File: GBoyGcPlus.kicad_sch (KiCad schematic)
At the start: 45 parts, among them J2 Conn_01x06, J3 Left Stick, J4 Right Stick, SW1 RKA2SGG055SMTR LFS, SW2 RKA2SGG055SMTR LFS, SW3 RKA2SGG055SMTR LFS, SW4 RKA2SGG055SMTR LFS, SW5 RKA2SGG055SMTR LFS, SW6 RKA2SGG055SMTR LFS, SW7 RKA2SGG055SMTR LFS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

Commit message: Schematic only
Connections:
- net +3V3: now also J3.1, J4.1; no longer J3.5, J4.5
- net CX: now also J4.5; no longer J4.1
- net CY: now also J4.2; no longer J4.4
- net GND: now also J3.4, J4.4; no longer J3.2, J4.2
- net SX: now also J3.5; no longer J3.1
- net SY: now also J3.2; no longer J3.4
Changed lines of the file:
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@@
     (effects (font (size 1.27 1.27)) (justify left bottom))
   )
-  (label "SY" (at 556.26 375.92 90) (fields_autoplaced)
+  (label "SY" (at 551.18 378.46 0) (fields_autoplaced)
     (effects (font (size 1.27 1.27)) (justify left bottom))
   )
@@
     (effects (font (size 1.27 1.27)) (justify left bottom))
   )
-  (label "CY" (at 595.63 375.92 90) (fields_autoplaced)
+  (label "CY" (at 590.55 378.46 0) (fields_autoplaced)
     (effects (font (size 1.27 1.27)) (justify left bottom))
   )
@@
     (effects (font (size 1.27 1.27)) (justify left bottom))
   )
-  (label "SX" (at 548.64 375.92 90) (fields_autoplaced)
+  (label "SX" (at 558.8 379.73 0) (fields_autoplaced)
     (effects (font (size 1.27 1.27)) (justify left bottom))
   )
@@
     (effects (font (size 1.27 1.27)) (justify left bottom))
   )
-  (label "CX" (at 588.01 375.92 90) (fields_autoplaced)
+  (label "CX" (at 598.17 378.46 0) (fields_autoplaced)
     (effects (font (size 1.27 1.27)) (justify left bottom))
   )
@@
     )
   )
-  (symbol (lib_id "power:+3V3") (at 598.17 378.46 180) (unit 1)
-    (in_bom yes) (on_board yes) (dnp no) (fields_autoplaced)
-    (property "Reference" "#PWR09" (at 598.17 374.65 0)
-      (effects (font (size 1.27 1.27)) hide)
-    )
-    (property "Value" "+3V3" (at 598.17 383.54 0)
-      (effects (font (size 1.27 1.27)))
-    )
-    (property "Footprint" "" (at 598.17 378.46 0)
-      (effects (font (size 1.27 1.27)) hide)
-    )
-    (property "Datasheet" "" (at 598.17 378.46 0)
+  (symbol (lib_id "power:+3V3") (at 588.01 375.92 180) (unit 1)
+    (in_bom yes) (on_board yes) (dnp no) (fields_autoplaced)
+    (property "Reference" "#PWR09" (at 588.01 372.11 0)
+      (effects (font (size 1.27 1.27)) hide)
+    )
+    (property "Value" "+3V3" (at 588.01 381 0)
+      (effects (font (size 1.27 1.27)))
+    )
+    (property "Footprint" "" (at 588.01 375.92 0)
+      (effects (font (size 1.27 1.27)) hide)
+    )
+    (property "Datasheet" "" (at 588.01 375.92 0)
       (effects (font (size 1.27 1.27)) hide)
     )
@@
     )
   )
-  (symbol (lib_id "power:GND") (at 551.18 378.46 0) (unit 1)
-    (in_bom yes) (on_board yes) (dnp no) (fields_autoplaced)
-    (property "Reference" "#PWR06" (at 551.18 384.81 0)
-      (effects (font (size 1.27 1.27)) hide)
-    )
-    (property "Value" "GND" (at 551.18 383.54 0)
-      (effects (font (size 1.27 1.27)))
-    )
-    (property "Footprint" "" (at 551.18 378.46 0)
-      (effects (font (size 1.27 1.27)) hide)
-    )
-    (property "Datasheet" "" (at 551.18 378.46 0)
+  (symbol (lib_id "power:GND") (at 556.26 375.92 0) (unit 1)
+    (in_bom yes) (on_board yes) (dnp no) (fields_autoplaced)
+    (property "Reference" "#PWR06" (at 556.26 382.27 0)
+      (effects (font (size 1.27 1.27)) hide)
+    )
+    (property "Value" "GND" (at 556.26 381 0)
+      (effects (font (size 1.27 1.27)))
+    )
+    (property "Footprint" "" (at 556.26 375.92 0)
+      (effects (font (size 1.27 1.27)) hide)
+    )
+    (property "Datasheet" "" (at 556.26 375.92 0)
       (effects (font (size 1.27 1.27)) hide)
     )
@@
     )
   )
-  (symbol (lib_id "power:+3V3") (at 558.8 379.73 180) (unit 1)
-    (in_bom yes) (on_board yes) (dnp no) (fields_autoplaced)
-    (property "Reference" "#PWR07" (at 558.8 375.92 0)
-      (effects (font (size 1.27 1.27)) hide)
-    )
-    (property "Value" "+3V3" (at 558.8 384.81 0)
-      (effects (font (size 1.27 1.27)))
-    )
-    (property "Footprint" "" (at 558.8 379.73 0)
-      (effects (font (size 1.27 1.27)) hide)
-    )
-    (property "Datasheet" "" (at 558.8 379.73 0)
+  (symbol (lib_id "power:+3V3") (at 548.64 375.92 180) (unit 1)
+    (in_bom yes) (on_board yes) (dnp no) (fields_autoplaced)
+    (property "Reference" "#PWR07" (at 548.64 372.11 0)
+      (effects (font (size 1.27 1.27)) hide)
+    )
+    (property "Value" "+3V3" (at 548.64 381 0)
+      (effects (font (size 1.27 1.27)))
+    )
+    (property "Footprint" "" (at 548.64 375.92 0)
+      (effects (font (size 1.27 1.27)) hide)
+    )
+    (property "Datasheet" "" (at 548.64 375.92 0)
       (effects (font (size 1.27 1.27)) hide)
     )
@@
     )
   )
-  (symbol (lib_id "power:GND") (at 590.55 378.46 0) (unit 1)
-    (in_bom yes) (on_board yes) (dnp no) (fields_autoplaced)
-    (property "Reference" "#PWR08" (at 590.55 384.81 0)
-      (effects (font (size 1.27 1.27)) hide)
-    )
-    (property "Value" "GND" (at 590.55 383.54 0)
-      (effects (font (size 1.27 1.27)))
-    )
-    (property "Footprint" "" (at 590.55 378.46 0)
-      (effects (font (size 1.27 1.27)) hide)
-    )
-    (property "Datasheet" "" (at 590.55 378.46 0)
-      (effects (font (size 1.27 1.27)) hide)
-    )
+  (symbol (lib_id "power:GND") (at 595.63 375.92 0) (unit 1)
+    (in_bom yes) (on_board yes) (dnp no) (fields_autoplaced)
+    (property "Reference" "#PWR08" (at 595.63 382.27 0)
+      (effects (font (size 1.27 1.27)) hide)
+    )
+    (property "Value" "GND" (at 595.63 381 0)
+      (effects (font (size 1.27 1.27)))
+    )
+    (property "Footprint" "" (at 595.63 375.92 0)
+      (effects (font (size 1.27 1.27)) hide)
+    )
+    (property "Datasheet" "" (at 595.63 375.92 0)
+      (effects (font (size 1.27 1.27)) hide)
+    )

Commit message: Added gerber files
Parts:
- removed TP6, TP7, TP8: TestPoint, TestPoint:TestPoint_Pad_D1.0mm, symbol Connector:TestPoint
- added J1: Conn_01x06, Connector_PinSocket_1.27mm:PinSocket_1x06_P1.27mm_Vertical, symbol Connector_Generic:Conn_01x06
- U1: footprint GCPlus:SSOP28_MC_MCH-L -> GCPlus:SSOP28_MC_MCH
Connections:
- net +3V3: now also J1.2 (Pin_2)
- net DD: no longer SW7.2
- net DL: no longer SW5.2
- net DR: no longer SW6.2
- net DU: no longer SW8.2
- net GND: now also J1.3 (Pin_3); no longer SW5.4, SW6.4, SW7.4, SW8.4
- net MCLR: now also J1.1 (Pin_1)
- net PGC: now also J1.5 (Pin_5)
- net PGD: now also J1.4 (Pin_4)

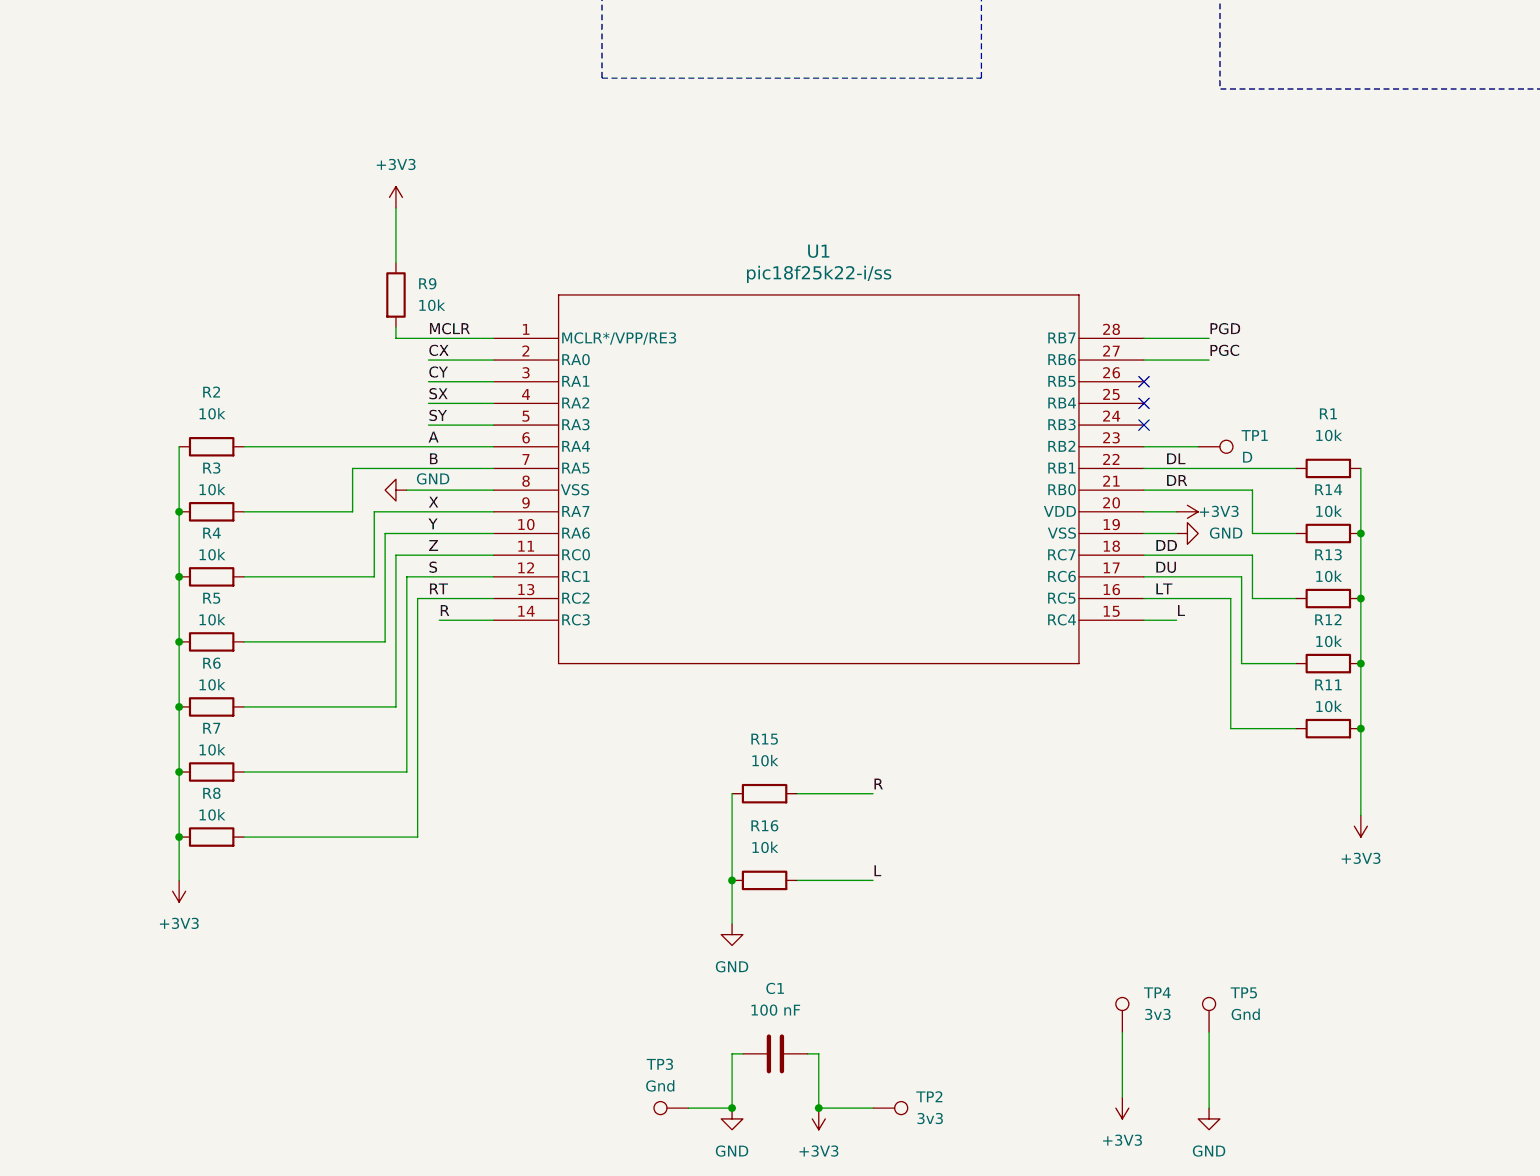
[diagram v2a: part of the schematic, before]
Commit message: Changed PCB to use GC2 Micro controller
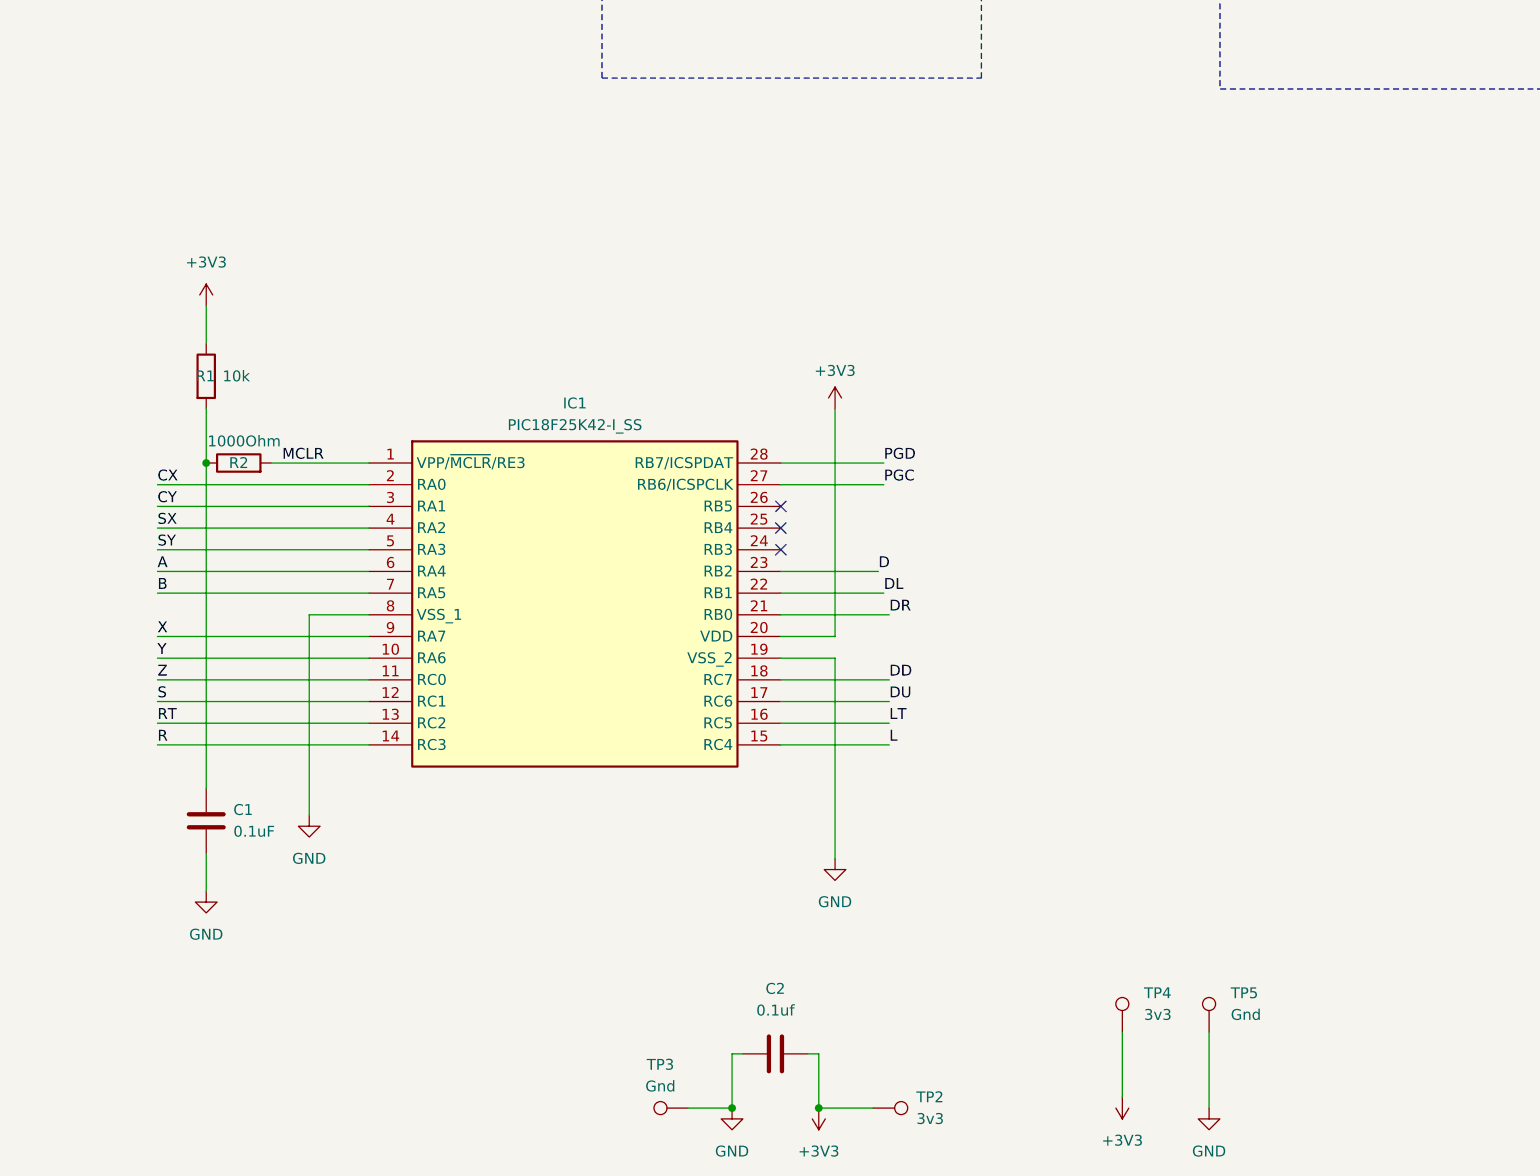
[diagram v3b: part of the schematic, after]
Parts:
- removed R11, R12, R13, R14, R15, R16, R3, R4, R5, R6, R7, R8, R9: 10k, Resistor_SMD:R_0603_1608Metric, symbol Device:R
- removed TP1: D, TestPoint:TestPoint_Pad_D1.0mm, symbol Connector:TestPoint
- removed U1: pic18f25k22-i/ss, GCPlus:SSOP28_MC_MCH, symbol GCPlus:pic18f25k22-i_ss
- added C1: 0.1uF, Capacitor_SMD:C_0402_1005Metric, symbol Device:C
- added IC1: PIC18F25K42-I_SS, GCPlus:SOP65P780X200-28N, symbol GCPlus:PIC18F25K42-I_SS
- C2: renamed from C1; value 100 nF -> 0.1uf; footprint Capacitor_SMD:C_0603_1608Metric -> Capacitor_SMD:C_0402_1005Metric
- R1: footprint Resistor_SMD:R_0603_1608Metric -> Resistor_SMD:R_0402_1005Metric
- R2: value 10k -> 1000Ohm; footprint Resistor_SMD:R_0603_1608Metric -> Resistor_SMD:R_0402_1005Metric
- SW5, SW6, SW7, SW8: footprint footprints:DPAD -> GCPlus:DPAD
- SW9: footprint footprints:RKA2SG_CNK -> GCPlus:RKA2SG_CNK-L
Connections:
- net +3V3: now also R1.1, IC1.20 (VDD); no longer R1.2, R2.1
- net A: now also IC1.6 (RA4); no longer R2.2
- net B: now also IC1.7 (RA5)
- net CX: now also IC1.2 (RA0)
- net CY: now also IC1.3 (RA1)
- net DD: now also IC1.18 (RC7)
- net DL: now also IC1.22 (RB1); no longer R1.1
- net DR: now also IC1.21 (RB0)
- net DU: now also IC1.17 (RC6)
- net GND: now also C1.2, IC1.19 (VSS_2), IC1.8 (VSS_1)
- net L: now also IC1.15 (RC4)
- net LT: now also IC1.16 (RC5)
- net MCLR: now also R2.2, IC1.1 (VPP/~{MCLR}/RE3)
- net PGC: now also IC1.27 (RB6/ICSPCLK)
- net PGD: now also IC1.28 (RB7/ICSPDAT)
- net R: now also IC1.14 (RC3)
- net RT: now also IC1.13 (RC2)
- net S: now also IC1.12 (RC1)
- net SX: now also IC1.4 (RA2)
- net SY: now also IC1.5 (RA3)
- net X: now also IC1.9 (RA7)
- net Y: now also IC1.10 (RA6)
- net Z: now also IC1.11 (RC0)
- new net: C1.1, R1.2, R2.1
- new net D: IC1.23 (RB2)
